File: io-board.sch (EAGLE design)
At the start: 25 parts

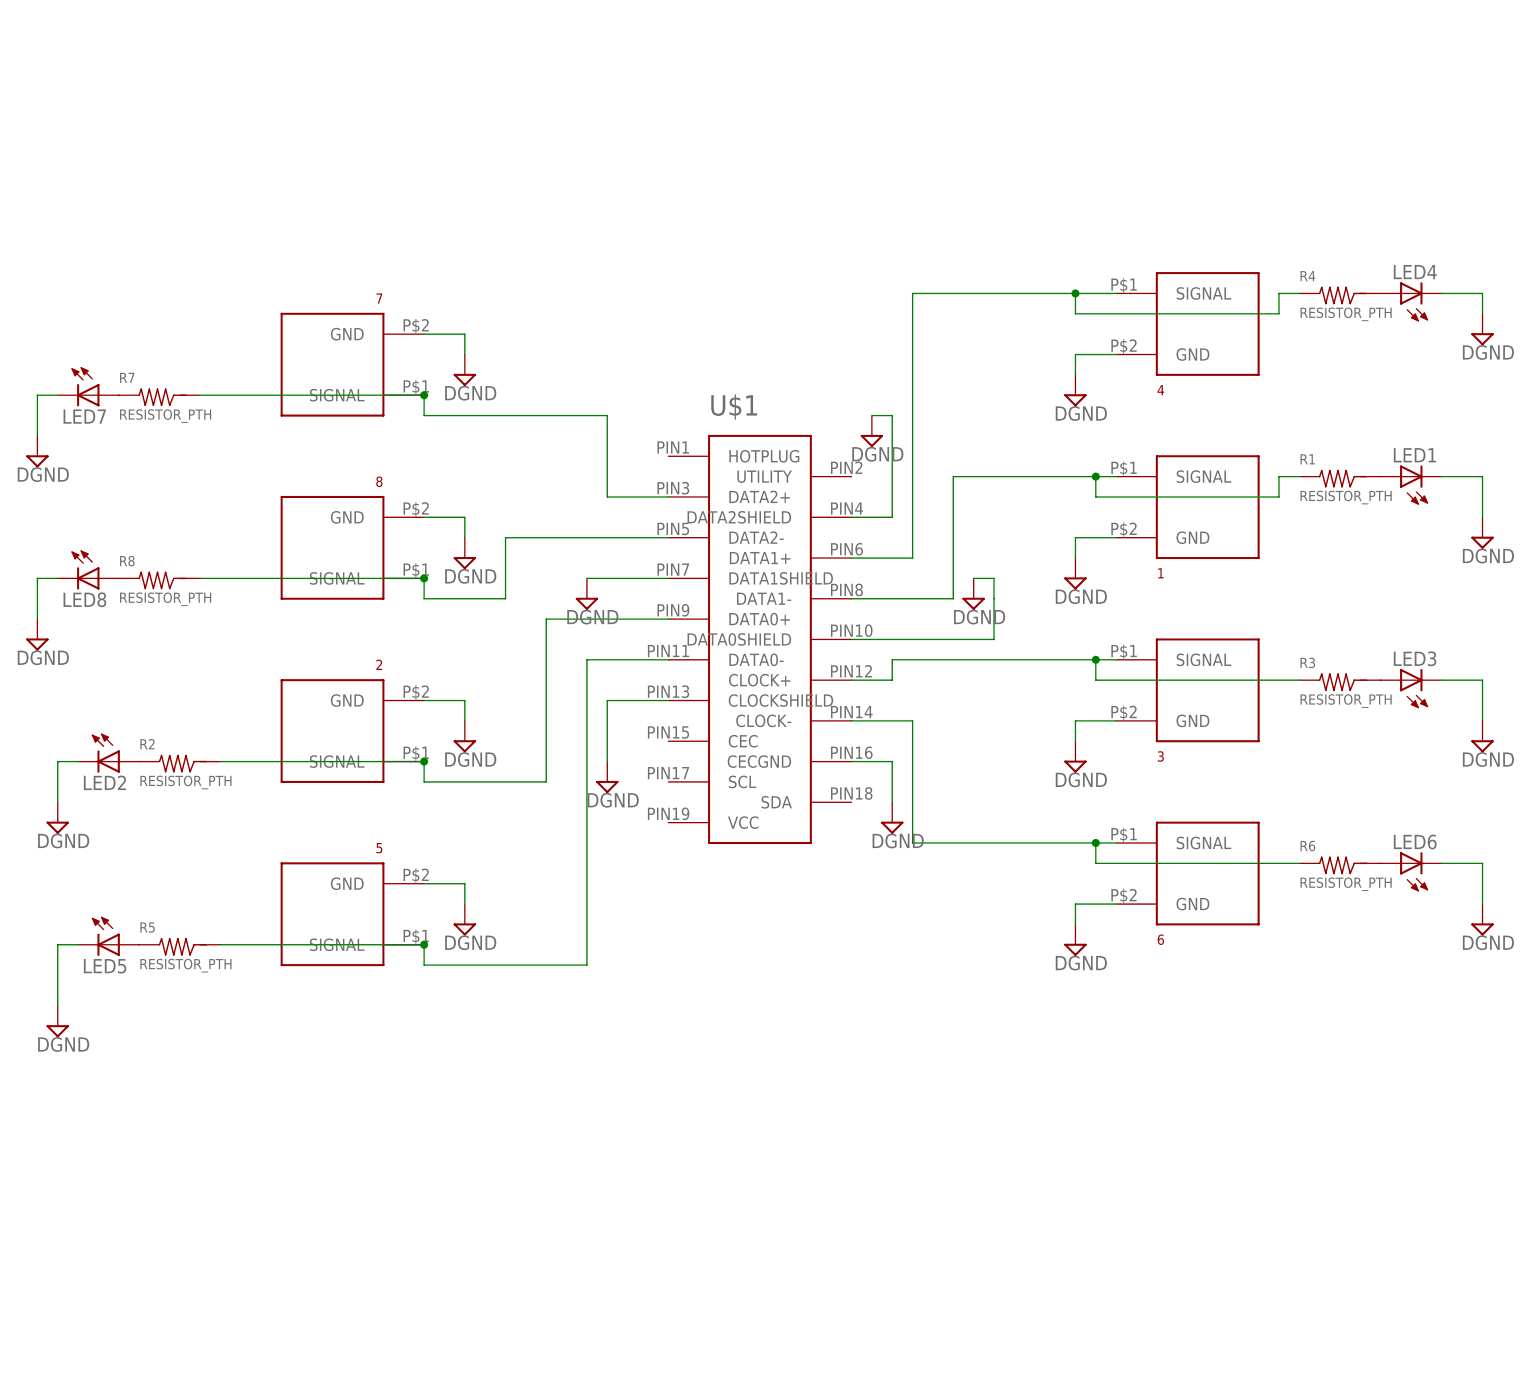
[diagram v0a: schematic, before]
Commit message: Make rackmount board the default
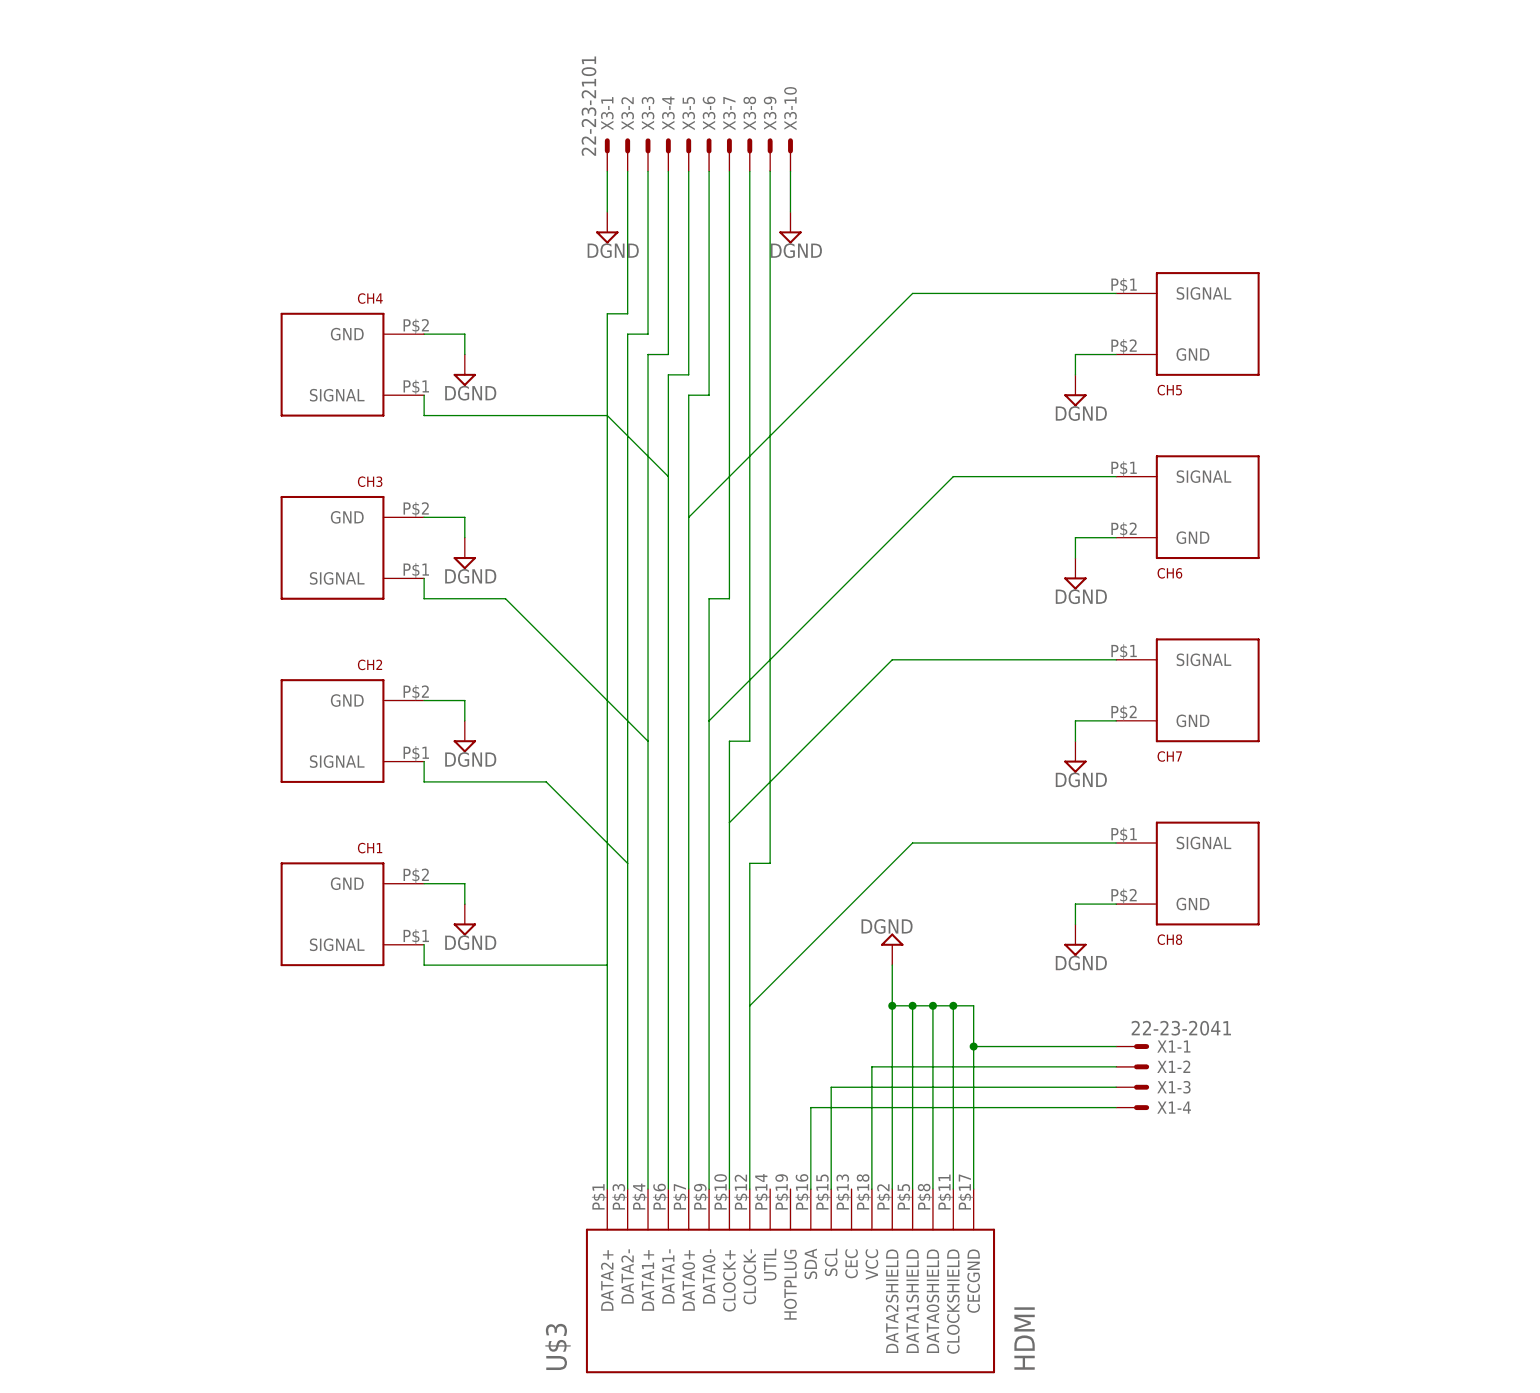
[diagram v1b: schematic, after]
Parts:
- removed LED1, LED2, LED3, LED4, LED5, LED6, LED7, LED8: (no value), sparkfun:LED3MM
- removed R1, R2, R3, R4, R5, R6, R7, R8: RESISTOR_PTH, josh:RESISTOR_PTH
- removed U$1: (no value), voigts:HDMI-D
- added U$3: HDMI, open-ephys:HDMI
- added X1: 22-23-2041, con-molex:22-23-2041
- added X3: 22-23-2101, con-molex:22-23-2101
- renumbered 1 to CH6, 2 to CH2, 3 to CH7, 4 to CH5, 5 to CH1, 6 to CH8, 7 to CH4, 8 to CH3
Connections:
- removed net N$1: LED6.A, R6.P$2
- removed net N$10: LED1.A, R1.P$2
- removed net N$11: LED4.A, R4.P$2
- removed net N$12: LED7.A, R7.P$1
- removed net N$13: LED8.A, R8.P$1
- removed net N$14: LED2.A, R2.P$1
- removed net N$15: LED5.A, R5.P$1
- removed net N$6: CH6.SIGNAL, R1.P$1, U$1.DATA1-
- removed net N$9: LED3.A, R3.P$2
- new net CH6: CH6.SIGNAL, U$3.DATA0-, X3-7.S
- new net I2C_CLK: U$3.SCL, X1-3.S
- new net I2C_DAT: U$3.SDA, X1-4.S
- new net VCC: U$3.VCC, X1-2.S
- net DGND: now also U$3.CECGND, U$3.CLOCKSHIELD, U$3.DATA0SHIELD, U$3.DATA1SHIELD, U$3.DATA2SHIELD, X1-1.S, X3-1.S, X3-10.S; no longer LED1.C, LED2.C, LED3.C, LED4.C, LED5.C, LED6.C, LED7.C, LED8.C, U$1.CECGND, U$1.CLOCKSHIELD, U$1.DATA0SHIELD, U$1.DATA1SHIELD, U$1.DATA2SHIELD
- net N$2: now also U$3.DATA1+, X3-4.S; no longer R8.P$2, U$1.DATA2-
- net N$23: now also U$3.DATA1-, X3-5.S; no longer R7.P$2, U$1.DATA2+
- net N$3: now also U$3.DATA2-, X3-3.S; no longer R2.P$2, U$1.DATA0+
- net N$4: now also U$3.DATA2+, X3-2.S; no longer R5.P$2, U$1.DATA0-
- net N$5: now also U$3.DATA0+, X3-6.S; no longer R4.P$1, U$1.DATA1+
- net N$7: now also U$3.CLOCK+, X3-8.S; no longer R3.P$1, U$1.CLOCK+
- net N$8: now also U$3.CLOCK-, X3-9.S; no longer R6.P$1, U$1.CLOCK-

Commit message: Add Illustrator file
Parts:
- renumbered U$3 to HDMI
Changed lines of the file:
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@@
 <part name="CH3" library="josh" deviceset="BNC_VERTICAL" device=""/>
 <part name="CH4" library="josh" deviceset="BNC_VERTICAL" device=""/>
-<part name="U$3" library="open-ephys" deviceset="HDMI" device=""/>
+<part name="HDMI" library="open-ephys" deviceset="HDMI" device=""/>
 <part name="X1" library="con-molex" deviceset="22-23-2041" device=""/>
 <part name="X3" library="con-molex" deviceset="22-23-2101" device=""/>
@@
 <instance part="CH3" gate="G$1" x="7.62" y="68.58" rot="R180"/>
 <instance part="CH4" gate="G$1" x="7.62" y="91.44" rot="R180"/>
-<instance part="U$3" gate="G$1" x="60.96" y="-22.86" rot="R90"/>
+<instance part="HDMI" gate="G$1" x="60.96" y="-22.86" rot="R90"/>
 <instance part="X1" gate="-1" x="106.68" y="0"/>
 <instance part="X1" gate="-2" x="106.68" y="-2.54"/>
@@
 <wire x1="17.78" y1="55.88" x2="17.78" y2="58.42" width="0.1524" layer="91"/>
 <pinref part="CH3" gate="G$1" pin="SIGNAL"/>
-<pinref part="U$3" gate="G$1" pin="DATA1+"/>
+<pinref part="HDMI" gate="G$1" pin="DATA1+"/>
 <wire x1="45.72" y1="38.1" x2="45.72" y2="86.36" width="0.1524" layer="91"/>
 <pinref part="X3" gate="-4" pin="S"/>
@@
 <wire x1="17.78" y1="33.02" x2="17.78" y2="35.56" width="0.1524" layer="91"/>
 <pinref part="CH2" gate="G$1" pin="SIGNAL"/>
-<pinref part="U$3" gate="G$1" pin="DATA2-"/>
+<pinref part="HDMI" gate="G$1" pin="DATA2-"/>
 <wire x1="43.18" y1="22.86" x2="43.18" y2="88.9" width="0.1524" layer="91"/>
 <pinref part="X3" gate="-3" pin="S"/>
@@
 <wire x1="17.78" y1="10.16" x2="17.78" y2="12.7" width="0.1524" layer="91"/>
 <pinref part="CH1" gate="G$1" pin="SIGNAL"/>
-<pinref part="U$3" gate="G$1" pin="DATA2+"/>
+<pinref part="HDMI" gate="G$1" pin="DATA2+"/>
 <wire x1="40.64" y1="10.16" x2="40.64" y2="91.44" width="0.1524" layer="91"/>
 <pinref part="X3" gate="-2" pin="S"/>
@@
 <wire x1="50.8" y1="66.04" x2="50.8" y2="-17.78" width="0.1524" layer="91"/>
 <pinref part="CH5" gate="G$1" pin="SIGNAL"/>
-<pinref part="U$3" gate="G$1" pin="DATA0+"/>
+<pinref part="HDMI" gate="G$1" pin="DATA0+"/>
 <wire x1="50.8" y1="66.04" x2="50.8" y2="81.28" width="0.1524" layer="91"/>
 <pinref part="X3" gate="-6" pin="S"/>
@@
 <wire x1="53.34" y1="40.64" x2="53.34" y2="-17.78" width="0.1524" layer="91"/>
 <pinref part="CH6" gate="G$1" pin="SIGNAL"/>
-<pinref part="U$3" gate="G$1" pin="DATA0-"/>
+<pinref part="HDMI" gate="G$1" pin="DATA0-"/>
 <wire x1="53.34" y1="40.64" x2="53.34" y2="55.88" width="0.1524" layer="91"/>
 <pinref part="X3" gate="-7" pin="S"/>
@@
 <wire x1="55.88" y1="27.94" x2="55.88" y2="-17.78" width="0.1524" layer="91"/>
 <pinref part="CH7" gate="G$1" pin="SIGNAL"/>
-<pinref part="U$3" gate="G$1" pin="CLOCK+"/>
+<pinref part="HDMI" gate="G$1" pin="CLOCK+"/>
 <wire x1="55.88" y1="27.94" x2="55.88" y2="38.1" width="0.1524" layer="91"/>
 <pinref part="X3" gate="-8" pin="S"/>
@@
 <wire x1="58.42" y1="5.08" x2="58.42" y2="-17.78" width="0.1524" layer="91"/>
 <pinref part="CH8" gate="G$1" pin="SIGNAL"/>
-<pinref part="U$3" gate="G$1" pin="CLOCK-"/>
+<pinref part="HDMI" gate="G$1" pin="CLOCK-"/>
 <wire x1="58.42" y1="5.08" x2="58.42" y2="22.86" width="0.1524" layer="91"/>
 <pinref part="X3" gate="-9" pin="S"/>
@@
 <wire x1="76.2" y1="-17.78" x2="76.2" y2="5.08" width="0.1524" layer="91"/>
 <pinref part="SUPPLY9" gate="G$1" pin="DGND"/>
-<pinref part="U$3" gate="G$1" pin="CECGND"/>
+<pinref part="HDMI" gate="G$1" pin="CECGND"/>
 <wire x1="76.2" y1="5.08" x2="76.2" y2="10.16" width="0.1524" layer="91"/>
 <wire x1="76.2" y1="5.08" x2="78.74" y2="5.08" width="0.1524" layer="91"/>
@@
 <wire x1="83.82" y1="5.08" x2="86.36" y2="5.08" width="0.1524" layer="91"/>
 <wire x1="86.36" y1="5.08" x2="86.36" y2="0" width="0.1524" layer="91"/>
-<pinref part="U$3" gate="G$1" pin="CLOCKSHIELD"/>
+<pinref part="HDMI" gate="G$1" pin="CLOCKSHIELD"/>
 <wire x1="86.36" y1="0" x2="86.36" y2="-17.78" width="0.1524" layer="91"/>
 <wire x1="83.82" y1="5.08" x2="83.82" y2="-17.78" width="0.1524" layer="91"/>
-<pinref part="U$3" gate="G$1" pin="DATA0SHIELD"/>
+<pinref part="HDMI" gate="G$1" pin="DATA0SHIELD"/>
 <wire x1="81.28" y1="-17.78" x2="81.28" y2="5.08" width="0.1524" layer="91"/>
-<pinref part="U$3" gate="G$1" pin="DATA1SHIELD"/>
+<pinref part="HDMI" gate="G$1" pin="DATA1SHIELD"/>
 <wire x1="78.74" y1="-17.78" x2="78.74" y2="5.08" width="0.1524" layer="91"/>
 <junction x="78.74" y="5.08"/>
@@
 <junction x="81.28" y="5.08"/>
 <junction x="83.82" y="5.08"/>
-<pinref part="U$3" gate="G$1" pin="DATA2SHIELD"/>
+<pinref part="HDMI" gate="G$1" pin="DATA2SHIELD"/>
 <pinref part="X1" gate="-1" pin="S"/>
 <wire x1="104.14" y1="0" x2="86.36" y2="0" width="0.1524" layer="91"/>
@@
 <wire x1="17.78" y1="81.28" x2="17.78" y2="78.74" width="0.1524" layer="91"/>
 <pinref part="CH4" gate="G$1" pin="SIGNAL"/>
-<pinref part="U$3" gate="G$1" pin="DATA1-"/>
+<pinref part="HDMI" gate="G$1" pin="DATA1-"/>
 <wire x1="48.26" y1="71.12" x2="48.26" y2="83.82" width="0.1524" layer="91"/>
 <pinref part="X3" gate="-5" pin="S"/>
@@
 <segment>
 <pinref part="X1" gate="-2" pin="S"/>
-<pinref part="U$3" gate="G$1" pin="VCC"/>
+<pinref part="HDMI" gate="G$1" pin="VCC"/>
 <wire x1="104.14" y1="-2.54" x2="73.66" y2="-2.54" width="0.1524" layer="91"/>
 <wire x1="73.66" y1="-2.54" x2="73.66" y2="-17.78" width="0.1524" layer="91"/>
@@
 <segment>
 <pinref part="X1" gate="-3" pin="S"/>
-<pinref part="U$3" gate="G$1" pin="SCL"/>
+<pinref part="HDMI" gate="G$1" pin="SCL"/>
 <wire x1="104.14" y1="-5.08" x2="68.58" y2="-5.08" width="0.1524" layer="91"/>
 <wire x1="68.58" y1="-5.08" x2="68.58" y2="-17.78" width="0.1524" layer="91"/>
@@
 <segment>
 <pinref part="X1" gate="-4" pin="S"/>
-<pinref part="U$3" gate="G$1" pin="SDA"/>
+<pinref part="HDMI" gate="G$1" pin="SDA"/>
 <wire x1="104.14" y1="-7.62" x2="66.04" y2="-7.62" width="0.1524" layer="91"/>
 <wire x1="66.04" y1="-7.62" x2="66.04" y2="-17.78" width="0.1524" layer="91"/>
